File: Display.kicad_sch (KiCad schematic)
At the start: 8 parts, among them U4 X1000, U9 TFP410PAP

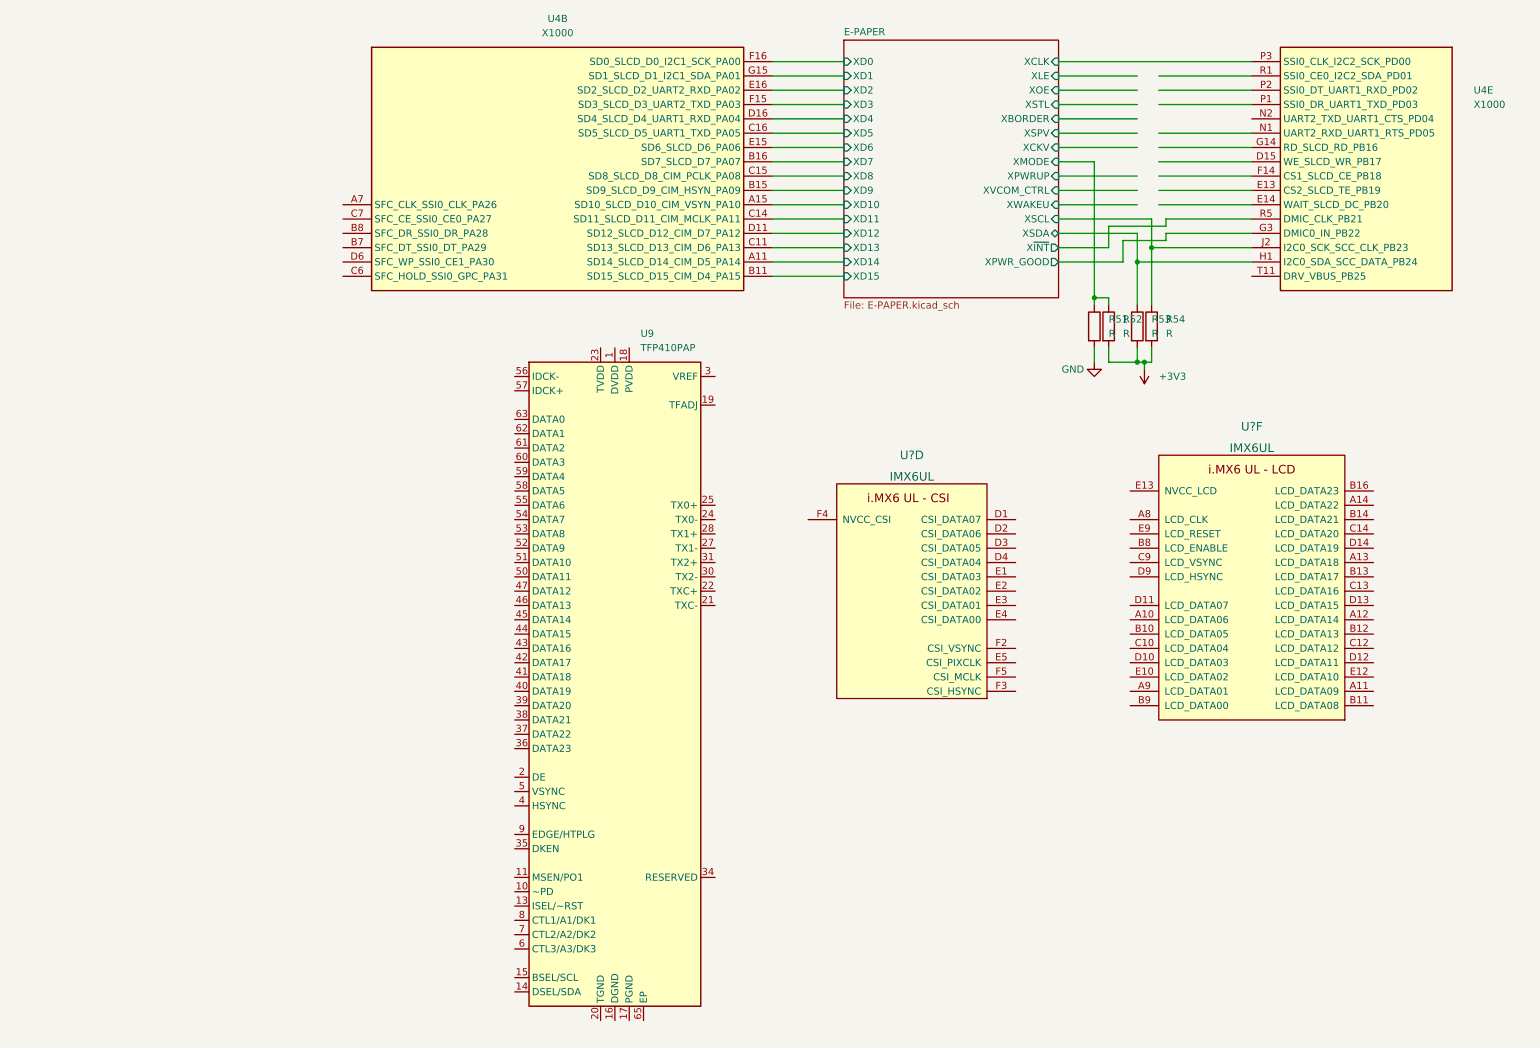
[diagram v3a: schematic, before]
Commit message: Display Update
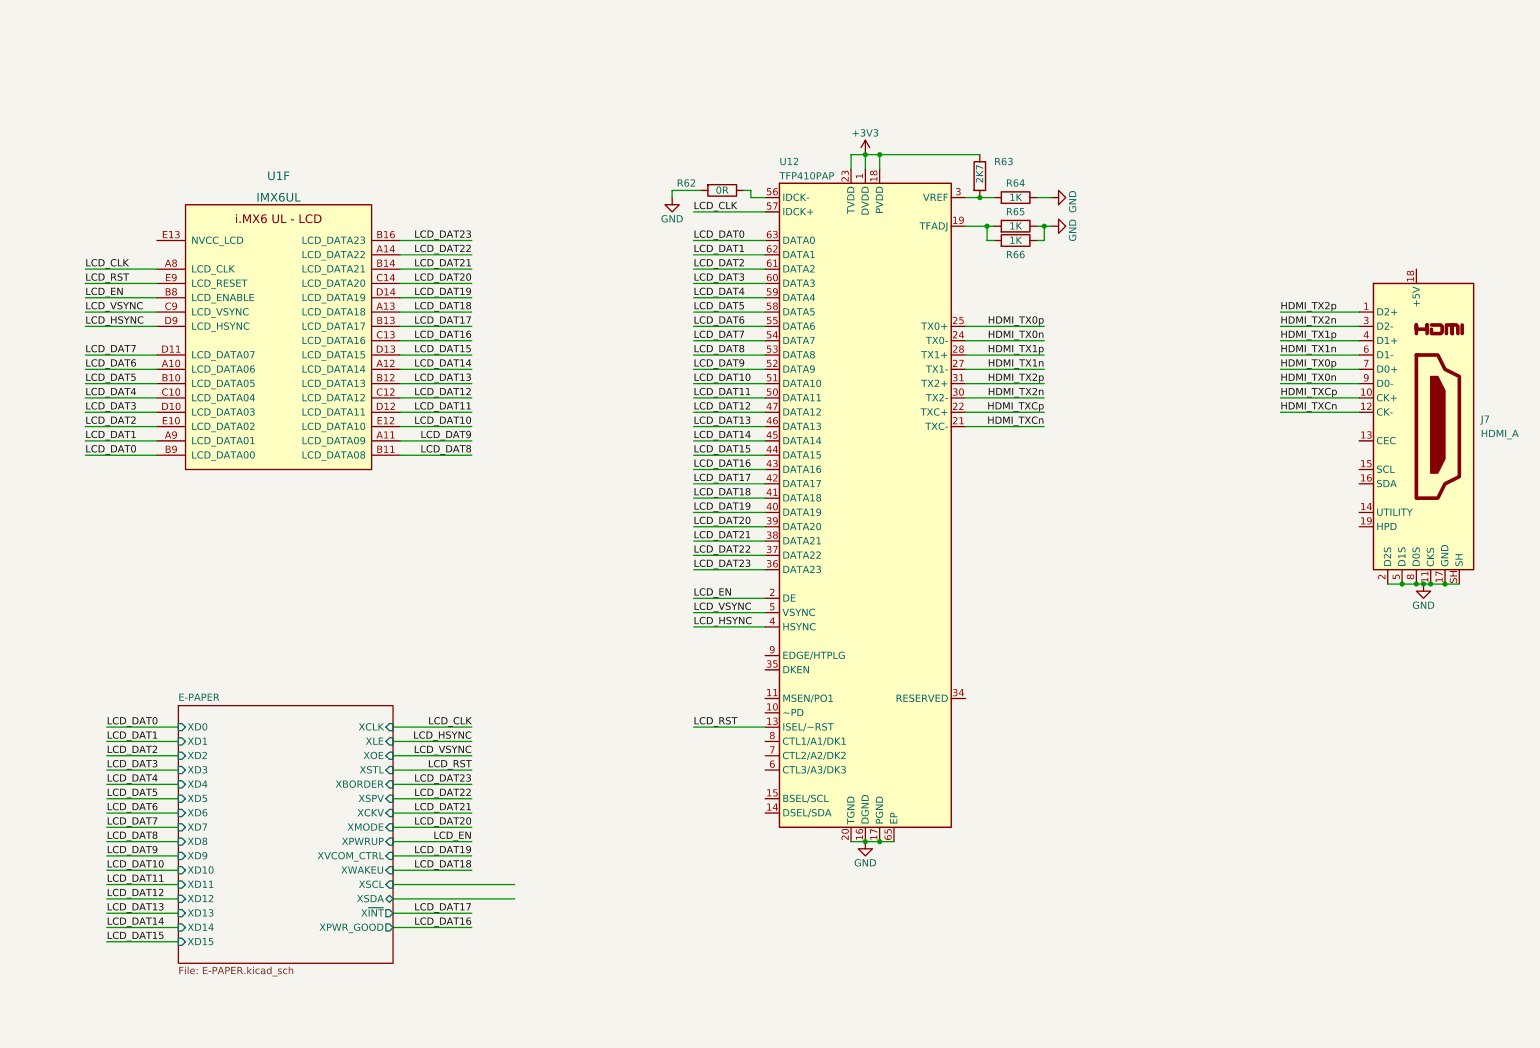
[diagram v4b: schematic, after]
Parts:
- removed R51, R52, R53, R54: R, symbol Device:R
- removed U4: X1000, TheBrutzlers_Lib:BGA256C80P16X16_1300X1300X130N, symbol TheBrutzlers_Lib:X1000
- removed U?: IMX6UL, TheBrutzlers_Lib:IMX6UL_BGA289, symbol TheBrutzlers_Lib:IMX6UL
- added J7: HDMI_A, Connector_HDMI:HDMI_A_Molex_208658-1001_Horizontal, symbol Connector:HDMI_A
- added R62: 0R, symbol Device:R
- added R63: 2K7, Resistor_SMD:R_0402_1005Metric, symbol Device:R
- added R64, R65, R66: 1K, symbol Device:R
- U12: renamed from U9; footprint Package_QFP:HTQFP-64-1EP_10x10mm_P0.5mm_EP8x8mm_Mask4.4x4.4mm_ThermalVias -> Package_QFP:HTQFP-64-1EP_10x10mm_P0.5mm_EP8x8mm
- gave numbers to parts that had none: 1
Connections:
- net +3V3: now also U12.1 (DVDD), U12.12 (DVDD), U12.18 (PVDD), U12.23 (TVDD), U12.29 (TVDD), U12.33 (DVDD), R63.1
- net GND: now also U12.16 (DGND), U12.17 (PGND), U12.20 (TGND), U12.26 (TGND), U12.32 (TGND), U12.48 (DGND), U12.64 (DGND), U12.65 (EP), J7.11 (CKS), J7.17 (GND), J7.2 (D2S), J7.5 (D1S), J7.8 (D0S), J7.SH, R62.2, R64.1, R65.1, R66.1
- net LCD_DAT6: now reaches U1.A10 (LCD_DATA06)
- net LCD_DAT6: now also U12.55 (DATA6)
- net LCD_DAT9: now reaches U1.A11 (LCD_DATA09)
- net LCD_DAT9: now also U12.52 (DATA9)
- net LCD_DAT14: now reaches U1.A12 (LCD_DATA14)
- net LCD_DAT14: now also U12.45 (DATA14)
- net LCD_DAT18: now reaches U1.A13 (LCD_DATA18)
- net LCD_DAT18: now also U12.41 (DATA18)
- net LCD_DAT22: now reaches U1.A14 (LCD_DATA22)
- net LCD_DAT22: now also U12.37 (DATA22)
- net LCD_CLK: now reaches U1.A8 (LCD_CLK)
- net LCD_CLK: now also U12.57 (IDCK+)
- net LCD_DAT1: now reaches U1.A9 (LCD_DATA01)
- net LCD_DAT1: now also U12.62 (DATA1)
- net LCD_DAT5: now reaches U1.B10 (LCD_DATA05)
- net LCD_DAT5: now also U12.58 (DATA5)
- net LCD_DAT8: now reaches U1.B11 (LCD_DATA08)
- net LCD_DAT8: now also U12.53 (DATA8)
- net LCD_DAT13: now reaches U1.B12 (LCD_DATA13)
- net LCD_DAT13: now also U12.46 (DATA13)
- net LCD_DAT17: now reaches U1.B13 (LCD_DATA17)
- net LCD_DAT17: now also U12.42 (DATA17)
- net LCD_DAT21: now reaches U1.B14 (LCD_DATA21)
- net LCD_DAT21: now also U12.38 (DATA21)
- net LCD_DAT23: now reaches U1.B16 (LCD_DATA23)
- net LCD_DAT23: now also U12.36 (DATA23)
- net LCD_EN: now reaches U1.B8 (LCD_ENABLE)
- net LCD_EN: now also U12.2 (DE)
- net LCD_DAT0: now reaches U1.B9 (LCD_DATA00)
- net LCD_DAT0: now also U12.63 (DATA0)
- net LCD_DAT4: now reaches U1.C10 (LCD_DATA04)
- net LCD_DAT4: now also U12.59 (DATA4)
- net LCD_DAT12: now reaches U1.C12 (LCD_DATA12)
- net LCD_DAT12: now also U12.47 (DATA12)
- net LCD_DAT16: now reaches U1.C13 (LCD_DATA16)
- net LCD_DAT16: now also U12.43 (DATA16)
- net LCD_DAT20: now reaches U1.C14 (LCD_DATA20)
- net LCD_DAT20: now also U12.39 (DATA20)
- net LCD_VSYNC: now reaches U1.C9 (LCD_VSYNC)
- net LCD_VSYNC: now also U12.5 (VSYNC)
- net LCD_DAT3: now reaches U1.D10 (LCD_DATA03)
- net LCD_DAT3: now also U12.60 (DATA3)
- net LCD_DAT7: now reaches U1.D11 (LCD_DATA07)
- net LCD_DAT7: now also U12.54 (DATA7)
- net LCD_DAT11: now reaches U1.D12 (LCD_DATA11)
- net LCD_DAT11: now also U12.50 (DATA11)
- net LCD_DAT15: now reaches U1.D13 (LCD_DATA15)
- net LCD_DAT15: now also U12.44 (DATA15)
- net LCD_DAT19: now reaches U1.D14 (LCD_DATA19)
- net LCD_DAT19: now also U12.40 (DATA19)
- net LCD_HSYNC: now reaches U1.D9 (LCD_HSYNC)
- net LCD_HSYNC: now also U12.4 (HSYNC)
- net LCD_DAT2: now reaches U1.E10 (LCD_DATA02)
- net LCD_DAT2: now also U12.61 (DATA2)
- net LCD_DAT10: now reaches U1.E12 (LCD_DATA10)
- net LCD_DAT10: now also U12.51 (DATA10)
- net LCD_RST: now reaches U1.E9 (LCD_RESET)
- net LCD_RST: now also U12.13 (ISEL/~RST)
- net at U12.19 (TFADJ): now also R65.2, R66.2
- net HDMI_TXCn: now reaches U12.21 (TXC-)
- net HDMI_TXCn: now also J7.12 (CK-)
- net HDMI_TXCp: now reaches U12.22 (TXC+)
- net HDMI_TXCp: now also J7.10 (CK+)
- net HDMI_TX0n: now reaches U12.24 (TX0-)
- net HDMI_TX0n: now also J7.9 (D0-)
- net HDMI_TX0p: now reaches U12.25 (TX0+)
- net HDMI_TX0p: now also J7.7 (D0+)
- net HDMI_TX1n: now reaches U12.27 (TX1-)
- net HDMI_TX1n: now also J7.6 (D1-)
- net HDMI_TX1p: now reaches U12.28 (TX1+)
- net HDMI_TX1p: now also J7.4 (D1+)
- net at U12.3 (VREF): now also R63.2, R64.2
- net HDMI_TX2n: now reaches U12.30 (TX2-)
- net HDMI_TX2n: now also J7.3 (D2-)
- net HDMI_TX2p: now reaches U12.31 (TX2+)
- net HDMI_TX2p: now also J7.1 (D2+)
- net at U12.56 (IDCK-): now also R62.1
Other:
- moved on the sheet: U12, U1F

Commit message: update DDR
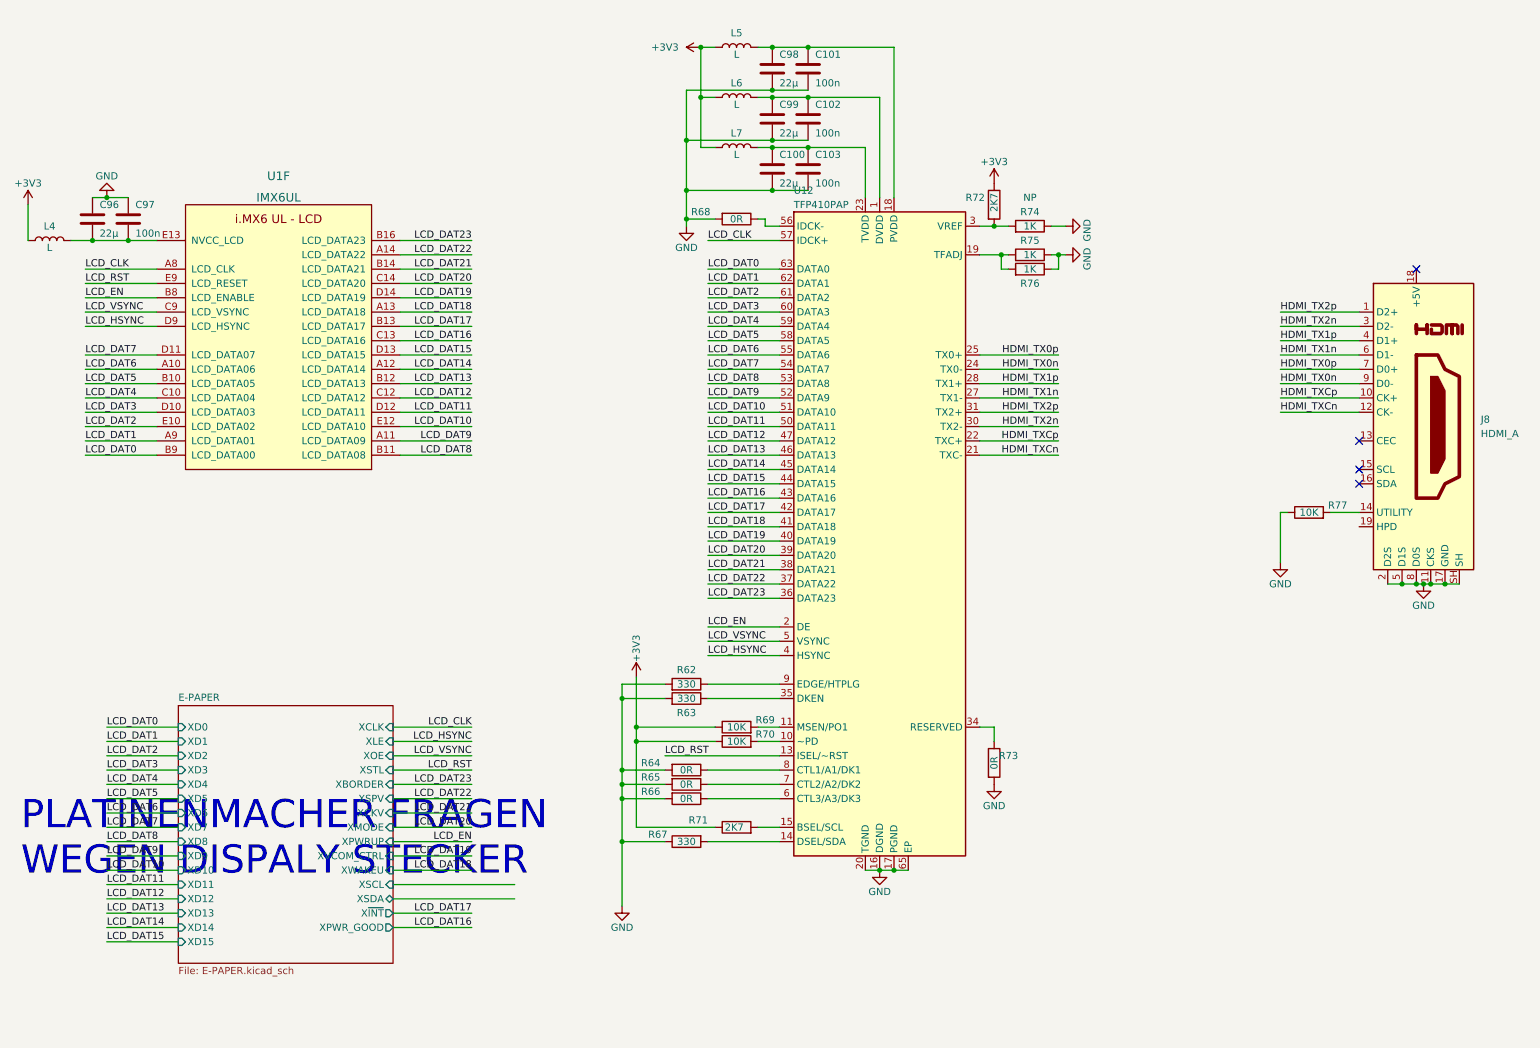
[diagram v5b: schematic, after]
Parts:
- added C100, C96, C98, C99: 22µ, Capacitor_SMD:C_0603_1608Metric, symbol Device:C
- added C101, C102, C103, C97: 100n, Capacitor_SMD:C_0402_1005Metric, symbol Device:C
- added L4, L5, L6, L7: L, symbol Device:L
- added R62, R63, R67: 330, Resistor_SMD:R_0402_1005Metric, symbol Device:R
- added R64, R65, R66, R73: 0R, symbol Device:R
- added R69, R70, R77: 10K, symbol Device:R
- added R71: 2K7, Resistor_SMD:R_0402_1005Metric, symbol Device:R
- R74: renamed from R64; NP (none) -> NP
- renumbered J7 to J8, R62 to R68, R63 to R72, R65 to R75, R66 to R76
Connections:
- net +3V3: now also L4.1, L5.1, L6.1, L7.1, R69.1, R70.1, R71.1; no longer U12.1 (DVDD), U12.12 (DVDD), U12.18 (PVDD), U12.23 (TVDD), U12.29 (TVDD), U12.33 (DVDD)
- net GND: now also C100.2, C101.2, C102.2, C103.2, C96.1, C97.1, C98.2, C99.2, R62.2, R63.2, R64.2, R65.2, R66.2, R67.1, R73.2, R77.1
- net at J8.14 (UTILITY): now also R77.2
- net at U1.E13 (NVCC_LCD): now also C96.2, C97.2, L4.2
- net at U12.10 (~PD): now also R70.2
- net at U12.11 (MSEN/PO1): now also R69.2
- net at U12.14 (DSEL/SDA): now also R67.2
- net at U12.15 (BSEL/SCL): now also R71.2
- net at U12.34 (RESERVED): now also R73.1
- net at U12.35 (DKEN): now also R63.1
- net at U12.6 (CTL3/A3/DK3): now also R66.1
- net at U12.7 (CTL2/A2/DK2): now also R65.1
- net at U12.8 (CTL1/A1/DK1): now also R64.1
- net at U12.9 (EDGE/HTPLG): now also R62.1
- new net: C102.1, C99.1, L6.2, U12.1 (DVDD), U12.12 (DVDD), U12.33 (DVDD)
- new net: C101.1, C98.1, L5.2, U12.18 (PVDD)
- new net: C100.1, C103.1, L7.2, U12.23 (TVDD), U12.29 (TVDD)
- no-connect marks 0 -> 4
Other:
- note added: "PLATINENMACHER FRAGEN WEGEN DISPALY STECKER"
- moved on the sheet: R68, R72, R74, R75, R76, U12
